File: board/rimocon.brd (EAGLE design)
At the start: 160 x 100 mm, 10 parts

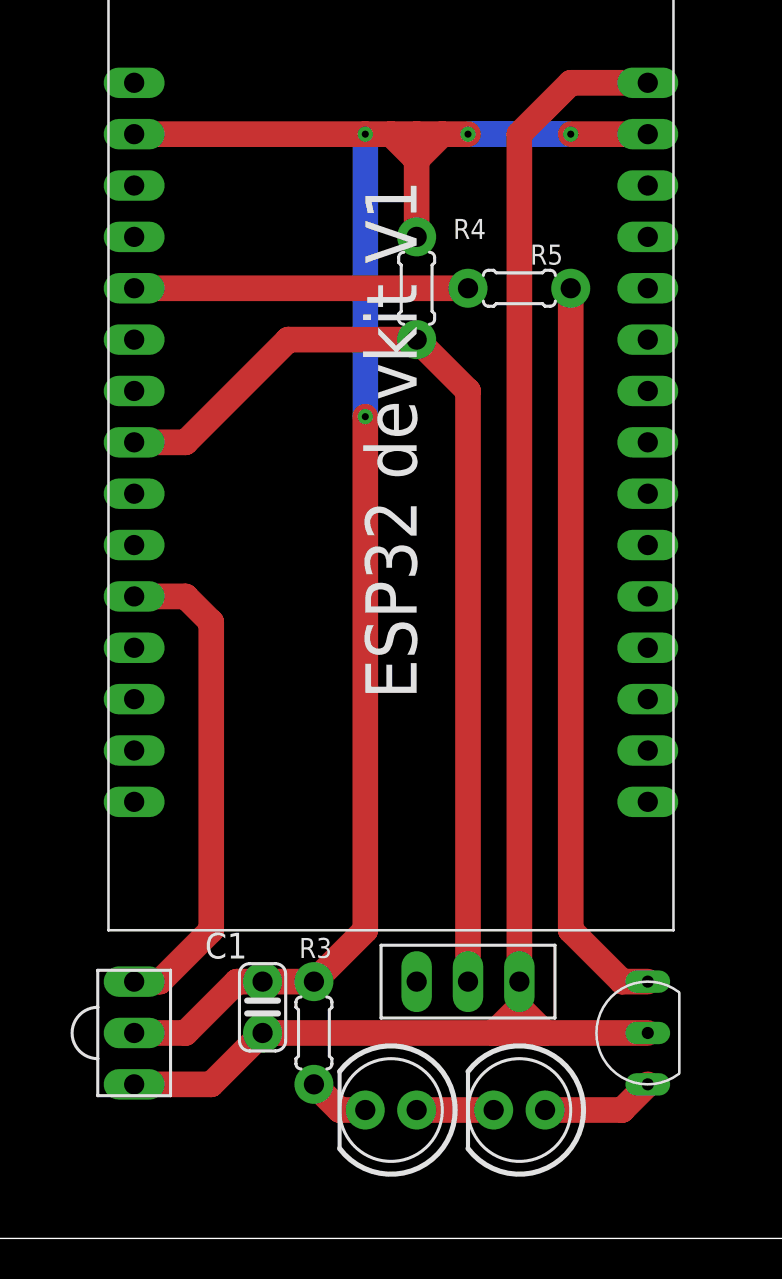
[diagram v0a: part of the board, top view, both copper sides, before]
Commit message: 送受信表示の統合とそれに伴う回路修正
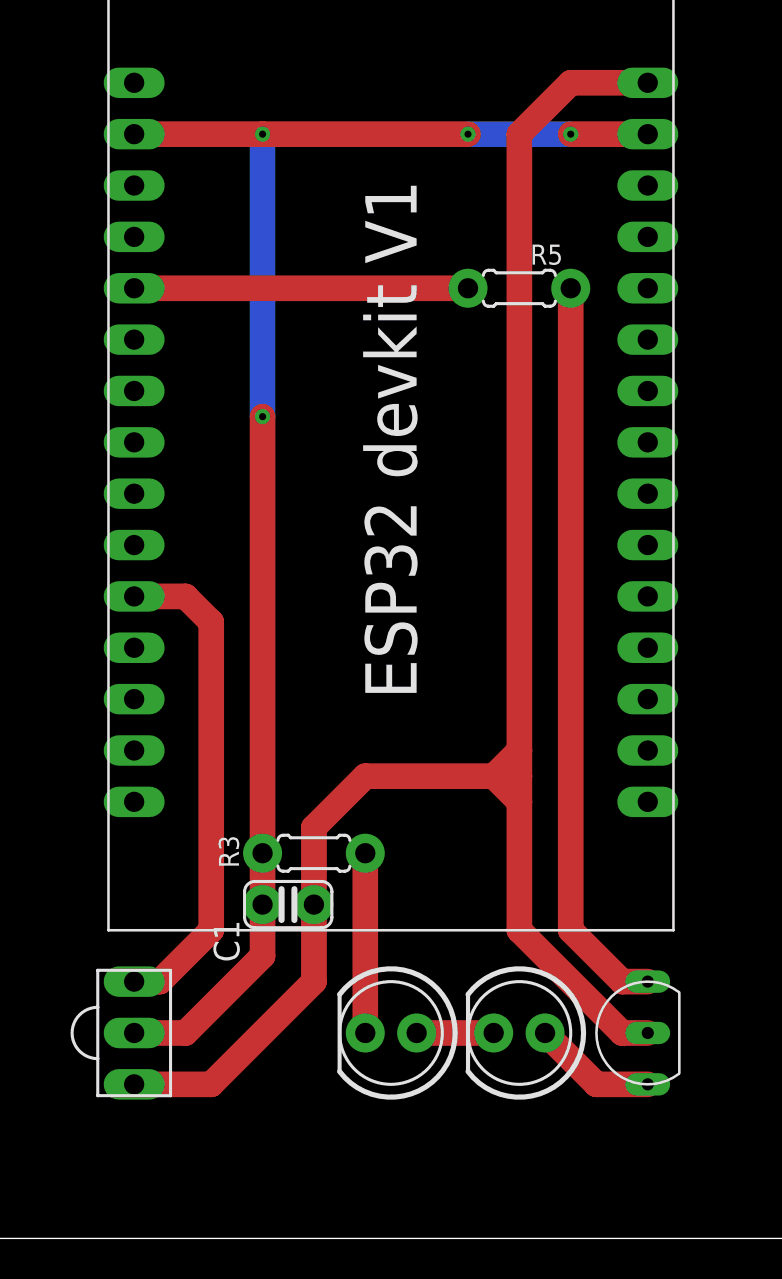
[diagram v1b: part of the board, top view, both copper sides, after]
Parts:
- removed R4: (no value), my_rcl:0204/5
- removed U$4: SWITCHSWTICH_SLIDE, Custom_Parts:SWITCH_SLIDE
- moved R3 8.89 mm to (34.3, 19.1), turned to 0 degrees
- moved C1 5.24 mm to (33.0, 16.5), turned to 180 degrees
- moved U$5 3.81 mm to (38.1, 10.2)
- moved U$6 3.81 mm to (44.5, 10.2)
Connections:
- removed net N$7: R4.2, U$3.D5, U$4.P$1
- net +5V: no longer U$4.P$2
- net GND: no longer R4.1
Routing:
- net N$7: track 48.9 -> 0.00 mm
- net GND: track 87.0 -> 74.0 mm
- net +5V: track 80.6 -> 88.6 mm
- net N$2: track 3.07 -> 8.89 mm
- net N$1: track 5.61 -> 6.13 mm
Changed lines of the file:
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@@
 <element name="U$3" library="Custom_IC" package="ESP32DEVKITV1" value="ESP32DEVKITV1" x="38.1" y="40.64" smashed="yes"/>
 <element name="U$2" library="Custom_Parts" package="OSRB38" value="OSRB38C9AA" x="25.4" y="10.16" smashed="yes" rot="R90"/>
-<element name="U$4" library="Custom_Parts" package="SWITCH_SLIDE" value="SWITCHSWTICH_SLIDE" x="41.91" y="12.7" smashed="yes" rot="R180"/>
-<element name="R3" library="my_rcl" package="0204/5" value="" x="34.29" y="10.16" smashed="yes" rot="R270">
-<attribute name="NAME" x="33.5534" y="13.8684" size="0.9906" layer="25" ratio="10"/>
-<attribute name="VALUE" x="31.9786" y="12.2936" size="0.9906" layer="27" ratio="10" rot="R270"/>
-</element>
-<element name="R4" library="my_rcl" package="0204/5" value="" x="39.37" y="46.99" smashed="yes" rot="R270">
-<attribute name="NAME" x="41.1734" y="49.4284" size="0.9906" layer="25" ratio="10"/>
-<attribute name="VALUE" x="37.0586" y="49.1236" size="0.9906" layer="27" ratio="10" rot="R270"/>
+<element name="R3" library="my_rcl" package="0204/5" value="" x="34.29" y="19.05" smashed="yes">
+<attribute name="NAME" x="30.5816" y="18.3134" size="0.9906" layer="25" ratio="10" rot="R90"/>
+<attribute name="VALUE" x="32.1564" y="16.7386" size="0.9906" layer="27" ratio="10"/>
 </element>
 <element name="R5" library="my_rcl" package="0204/5" value="" x="44.45" y="46.99" smashed="yes">
@@
 <attribute name="VALUE" x="42.3164" y="44.6786" size="0.9906" layer="27" ratio="10"/>
 </element>
-<element name="U$5" library="Custom_Parts" package="OSI5FU3A11C" value="LEDOSI5FU3A11C" x="38.1" y="6.35" smashed="yes" rot="R180"/>
-<element name="U$6" library="Custom_Parts" package="OSI5FU3A11C" value="LEDOSI5FU3A11C" x="44.45" y="6.35" smashed="yes" rot="R180"/>
-<element name="C1" library="my_rcl" package="C025-024X044" value="" x="31.75" y="11.43" smashed="yes" rot="R90">
-<attribute name="NAME" x="30.988" y="15.113" size="1.27" layer="25" ratio="10" rot="R180"/>
-<attribute name="VALUE" x="34.417" y="9.652" size="1.27" layer="27" ratio="10" rot="R90"/>
+<element name="U$5" library="Custom_Parts" package="OSI5FU3A11C" value="LEDOSI5FU3A11C" x="38.1" y="10.16" smashed="yes" rot="R180"/>
+<element name="U$6" library="Custom_Parts" package="OSI5FU3A11C" value="LEDOSI5FU3A11C" x="44.45" y="10.16" smashed="yes" rot="R180"/>
+<element name="C1" library="my_rcl" package="C025-024X044" value="" x="33.02" y="16.51" smashed="yes" rot="R180">
+<attribute name="NAME" x="29.337" y="15.748" size="1.27" layer="25" ratio="10" rot="R270"/>
+<attribute name="VALUE" x="34.798" y="19.177" size="1.27" layer="27" ratio="10" rot="R180"/>
 </element>
 </elements>
@@
 <contactref element="U$3" pad="GND@1"/>
 <contactref element="U$2" pad="GND"/>
-<wire x1="41.91" y1="54.61" x2="40.64" y2="54.61" width="1.27" layer="1"/>
-<wire x1="40.64" y1="54.61" x2="39.37" y2="54.61" width="1.27" layer="1"/>
-<wire x1="39.37" y1="54.61" x2="38.1" y2="54.61" width="1.27" layer="1"/>
-<wire x1="38.1" y1="54.61" x2="36.83" y2="54.61" width="1.27" layer="1"/>
-<wire x1="36.83" y1="54.61" x2="25.4" y2="54.61" width="1.27" layer="1"/>
-<wire x1="39.37" y1="54.61" x2="39.37" y2="53.34" width="1.27" layer="1"/>
-<via x="36.83" y="54.61" extent="1-16" drill="0.35"/>
-<wire x1="36.83" y1="54.61" x2="36.83" y2="40.64" width="1.27" layer="16"/>
-<via x="36.83" y="40.64" extent="1-16" drill="0.35"/>
-<wire x1="36.83" y1="15.24" x2="36.83" y2="40.64" width="1.27" layer="1"/>
+<wire x1="41.91" y1="54.61" x2="31.75" y2="54.61" width="1.27" layer="1"/>
+<wire x1="31.75" y1="54.61" x2="25.4" y2="54.61" width="1.27" layer="1"/>
+<via x="31.75" y="54.61" extent="1-16" drill="0.35"/>
+<wire x1="31.75" y1="54.61" x2="31.75" y2="40.64" width="1.27" layer="16"/>
+<via x="31.75" y="40.64" extent="1-16" drill="0.35"/>
 <via x="41.91" y="54.61" extent="1-16" drill="0.35"/>
 <wire x1="41.91" y1="54.61" x2="46.99" y2="54.61" width="1.27" layer="16"/>
 <wire x1="50.8" y1="54.61" x2="46.99" y2="54.61" width="1.27" layer="1"/>
 <via x="46.99" y="54.61" extent="1-16" drill="0.35"/>
-<wire x1="39.37" y1="53.34" x2="40.64" y2="54.61" width="1.27" layer="1"/>
-<wire x1="39.37" y1="53.34" x2="38.1" y2="54.61" width="1.27" layer="1"/>
 <contactref element="R3" pad="1"/>
-<contactref element="R4" pad="1"/>
 <contactref element="C1" pad="2"/>
-<wire x1="39.37" y1="49.53" x2="39.37" y2="53.34" width="1.27" layer="1"/>
 <wire x1="25.4" y1="10.16" x2="27.94" y2="10.16" width="1.27" layer="1"/>
-<wire x1="30.48" y1="12.7" x2="27.94" y2="10.16" width="1.27" layer="1"/>
-<wire x1="31.75" y1="12.7" x2="30.48" y2="12.7" width="1.27" layer="1"/>
-<wire x1="31.75" y1="12.7" x2="34.29" y2="12.7" width="1.27" layer="1"/>
-<wire x1="34.29" y1="12.7" x2="36.83" y2="15.24" width="1.27" layer="1"/>
+<wire x1="27.94" y1="10.16" x2="31.75" y2="13.97" width="1.27" layer="1"/>
+<wire x1="31.75" y1="13.97" x2="31.75" y2="19.05" width="1.27" layer="1"/>
+<wire x1="31.75" y1="40.64" x2="31.75" y2="19.05" width="1.27" layer="1"/>
+<wire x1="31.75" y1="19.05" x2="31.75" y2="16.51" width="0" layer="19" extent="1-1"/>
 </signal>
 <signal name="N$3">
@@
 <contactref element="U$3" pad="VIN"/>
 <contactref element="U$1" pad="C"/>
-<contactref element="U$4" pad="P$2"/>
 <wire x1="50.8" y1="57.15" x2="46.99" y2="57.15" width="1.27" layer="1"/>
-<wire x1="44.45" y1="11.43" x2="45.72" y2="10.16" width="1.27" layer="1"/>
-<wire x1="50.8" y1="10.16" x2="45.72" y2="10.16" width="1.27" layer="1"/>
-<wire x1="44.45" y1="12.7" x2="44.45" y2="11.43" width="1.27" layer="1"/>
+<wire x1="50.8" y1="10.16" x2="49.53" y2="10.16" width="1.27" layer="1"/>
 <wire x1="46.99" y1="57.15" x2="44.45" y2="54.61" width="1.27" layer="1"/>
-<wire x1="44.45" y1="12.7" x2="44.45" y2="54.61" width="1.27" layer="1"/>
-<wire x1="45.72" y1="10.16" x2="43.18" y2="10.16" width="1.27" layer="1"/>
-<wire x1="43.18" y1="10.16" x2="44.45" y2="11.43" width="1.27" layer="1"/>
 <contactref element="U$2" pad="VCC"/>
 <contactref element="C1" pad="1"/>
-<wire x1="31.75" y1="10.16" x2="29.21" y2="7.62" width="1.27" layer="1"/>
-<wire x1="25.4" y1="7.62" x2="29.21" y2="7.62" width="1.27" layer="1"/>
-<wire x1="31.75" y1="10.16" x2="43.18" y2="10.16" width="1.27" layer="1"/>
+<wire x1="29.21" y1="7.62" x2="25.4" y2="7.62" width="1.27" layer="1"/>
+<wire x1="44.45" y1="54.61" x2="44.45" y2="24.13" width="1.27" layer="1"/>
+<wire x1="44.45" y1="24.13" x2="44.45" y2="22.86" width="1.27" layer="1"/>
+<wire x1="44.45" y1="22.86" x2="44.45" y2="21.59" width="1.27" layer="1"/>
+<wire x1="44.45" y1="21.59" x2="44.45" y2="15.24" width="1.27" layer="1"/>
+<wire x1="44.45" y1="15.24" x2="49.53" y2="10.16" width="1.27" layer="1"/>
+<wire x1="34.29" y1="16.51" x2="34.29" y2="12.7" width="1.27" layer="1"/>
+<wire x1="34.29" y1="12.7" x2="29.21" y2="7.62" width="1.27" layer="1"/>
+<wire x1="34.29" y1="16.51" x2="34.29" y2="20.32" width="1.27" layer="1"/>
+<wire x1="34.29" y1="20.32" x2="36.83" y2="22.86" width="1.27" layer="1"/>
+<wire x1="36.83" y1="22.86" x2="43.18" y2="22.86" width="1.27" layer="1"/>
+<wire x1="43.18" y1="22.86" x2="44.45" y2="22.86" width="1.27" layer="1"/>
+<wire x1="43.18" y1="22.86" x2="44.45" y2="21.59" width="1.27" layer="1"/>
+<wire x1="43.18" y1="22.86" x2="44.45" y2="24.13" width="1.27" layer="1"/>
 </signal>
 <signal name="3V3">
@@
 <contactref element="R5" pad="2"/>
 <wire x1="46.99" y1="46.99" x2="46.99" y2="15.24" width="1.27" layer="1"/>
-</signal>
-<signal name="N$7">
-<contactref element="U$4" pad="P$1"/>
-<wire x1="41.91" y1="41.91" x2="41.91" y2="12.7" width="1.27" layer="1"/>
-<contactref element="U$3" pad="D5"/>
-<wire x1="25.4" y1="39.37" x2="27.94" y2="39.37" width="1.27" layer="1"/>
-<wire x1="33.02" y1="44.45" x2="27.94" y2="39.37" width="1.27" layer="1"/>
-<contactref element="R4" pad="2"/>
-<wire x1="39.37" y1="44.45" x2="41.91" y2="41.91" width="1.27" layer="1"/>
-<wire x1="39.37" y1="44.45" x2="33.02" y2="44.45" width="1.27" layer="1"/>
 </signal>
 <signal name="N$4">
@@
 <contactref element="U$5" pad="A"/>
 <contactref element="U$6" pad="K"/>
-<wire x1="43.18" y1="6.35" x2="39.37" y2="6.35" width="1.27" layer="1"/>
+<wire x1="43.18" y1="10.16" x2="39.37" y2="10.16" width="1.27" layer="1"/>
 </signal>
 <signal name="N$1">
 <contactref element="U$1" pad="E"/>
 <contactref element="U$6" pad="A"/>
-<wire x1="50.8" y1="7.62" x2="49.53" y2="6.35" width="1.27" layer="1"/>
-<wire x1="49.53" y1="6.35" x2="45.72" y2="6.35" width="1.27" layer="1"/>
+<wire x1="50.8" y1="7.62" x2="48.26" y2="7.62" width="1.27" layer="1"/>
+<wire x1="48.26" y1="7.62" x2="45.72" y2="10.16" width="1.27" layer="1"/>
 </signal>
 <signal name="N$2">
 <contactref element="U$5" pad="K"/>
 <contactref element="R3" pad="2"/>
-<wire x1="36.83" y1="6.35" x2="35.56" y2="6.35" width="1.27" layer="1"/>
-<wire x1="35.56" y1="6.35" x2="34.29" y2="7.62" width="1.27" layer="1"/>
+<wire x1="36.83" y1="10.16" x2="36.83" y2="19.05" width="1.27" layer="1"/>
 </signal>
 </signals>

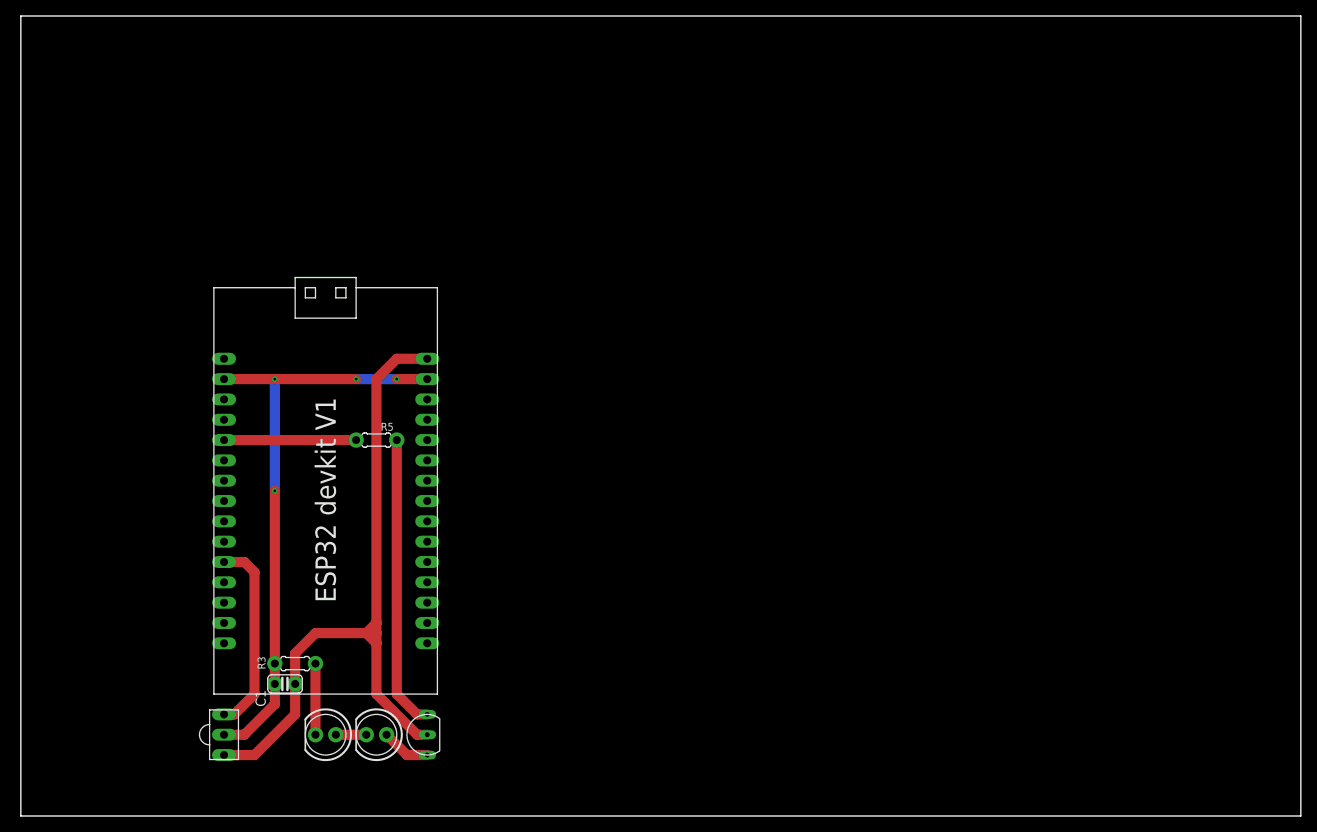
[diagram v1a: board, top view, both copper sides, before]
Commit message: 回路をエミッタ設置へと変更 単ボタンリモコン用繰り返し処理の実装
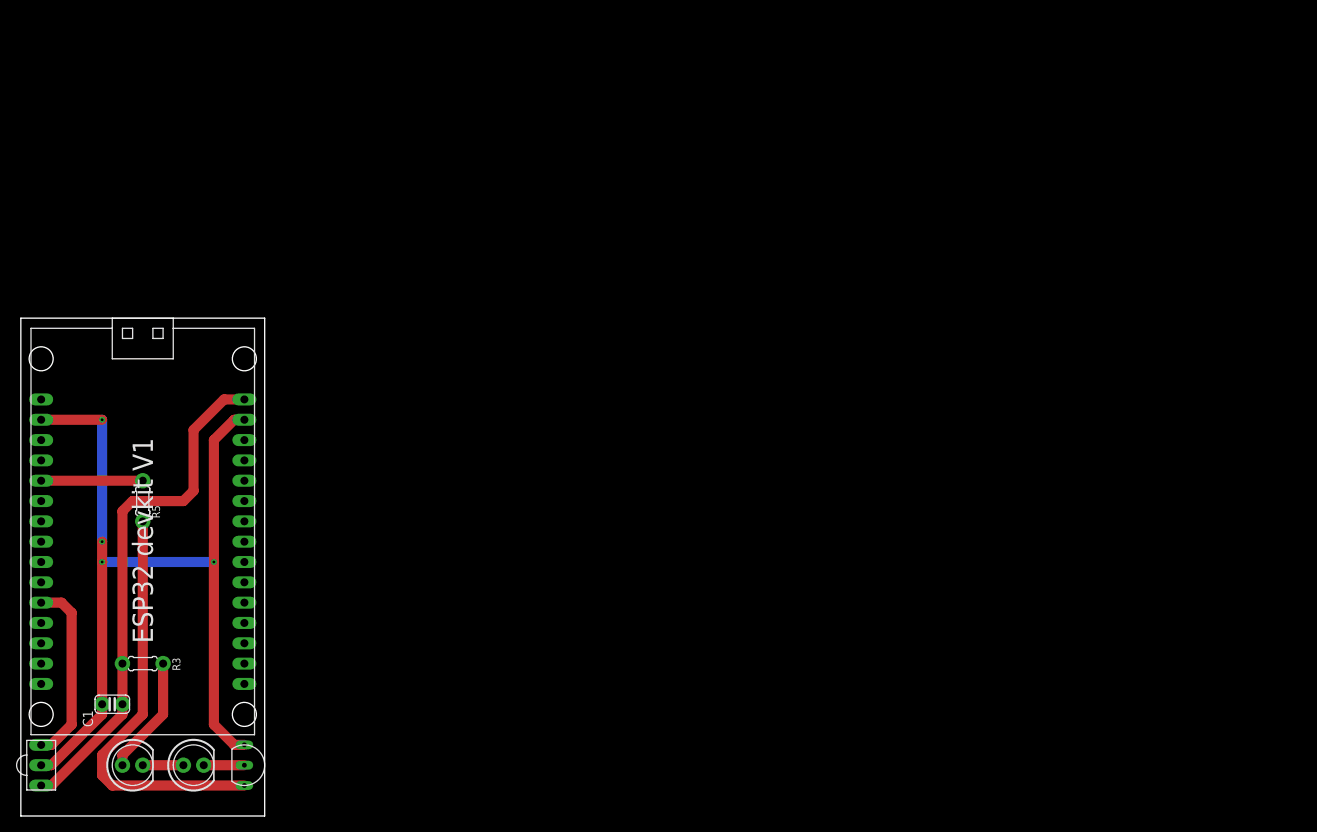
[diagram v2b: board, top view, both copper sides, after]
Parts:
- moved U$6 30.7 mm to (14.0, 6.35), turned to 0 degrees
- moved R5 30.2 mm to (15.2, 39.4), turned to 270 degrees
- moved U$3 23.4 mm to (15.2, 35.6)
- moved U$1 23.2 mm to (27.9, 6.35), turned to 90 degrees
- moved U$2 23.2 mm to (2.54, 6.35)
- moved C1 21.7 mm to (11.4, 14.0)
- moved R3 19.0 mm to (15.2, 19.1), turned to 180 degrees
- moved U$5 16.9 mm to (21.6, 6.35), turned to 0 degrees
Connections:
- net +5V: now also R3.2; no longer U$1.C
- net GND: now also U$1.E; no longer R3.1
- net N$1: now also U$1.C, U$5.K; no longer U$1.E, U$6.A
- net N$2: now also R3.1, U$6.A; no longer R3.2, U$5.K
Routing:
- net GND: track 74.0 -> 114.0 mm
- net +5V: track 88.6 -> 64.7 mm
- net N$6: track 36.6 -> 52.2 mm
- net N$2: track 8.89 -> 14.8 mm
- net N$3: track 16.5 -> 12.7 mm
- net N$4: track 24.4 -> 23.2 mm
- net N$8: track 3.81 -> 5.08 mm
- net N$1: track 6.13 -> 5.08 mm
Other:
- board size 160 x 100 mm -> 30.5 x 62.2 mm
